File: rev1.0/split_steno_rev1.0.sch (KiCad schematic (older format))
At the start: 45 parts, among them J0 Audio-Jack-4, K0 KEYSW, K1 KEYSW, K10 KEYSW, K11 KEYSW, K12 KEYSW, K13 KEYSW, K14 KEYSW, K15 KEYSW, K16 KEYSW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

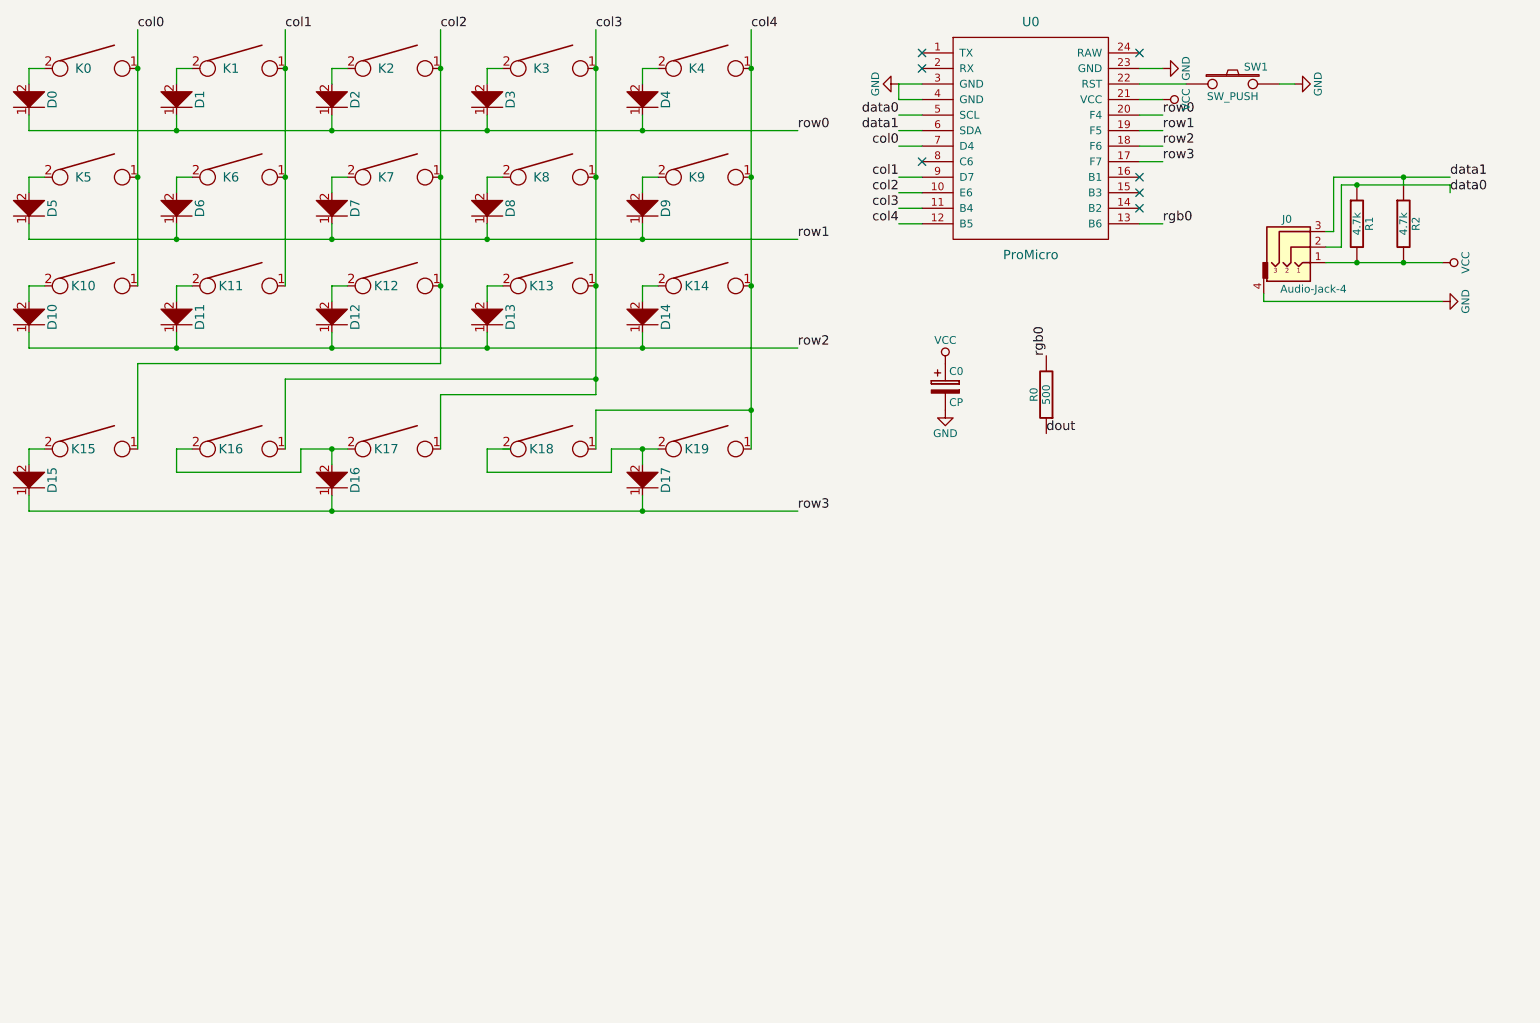
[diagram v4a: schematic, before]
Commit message: updated schematic and footprints
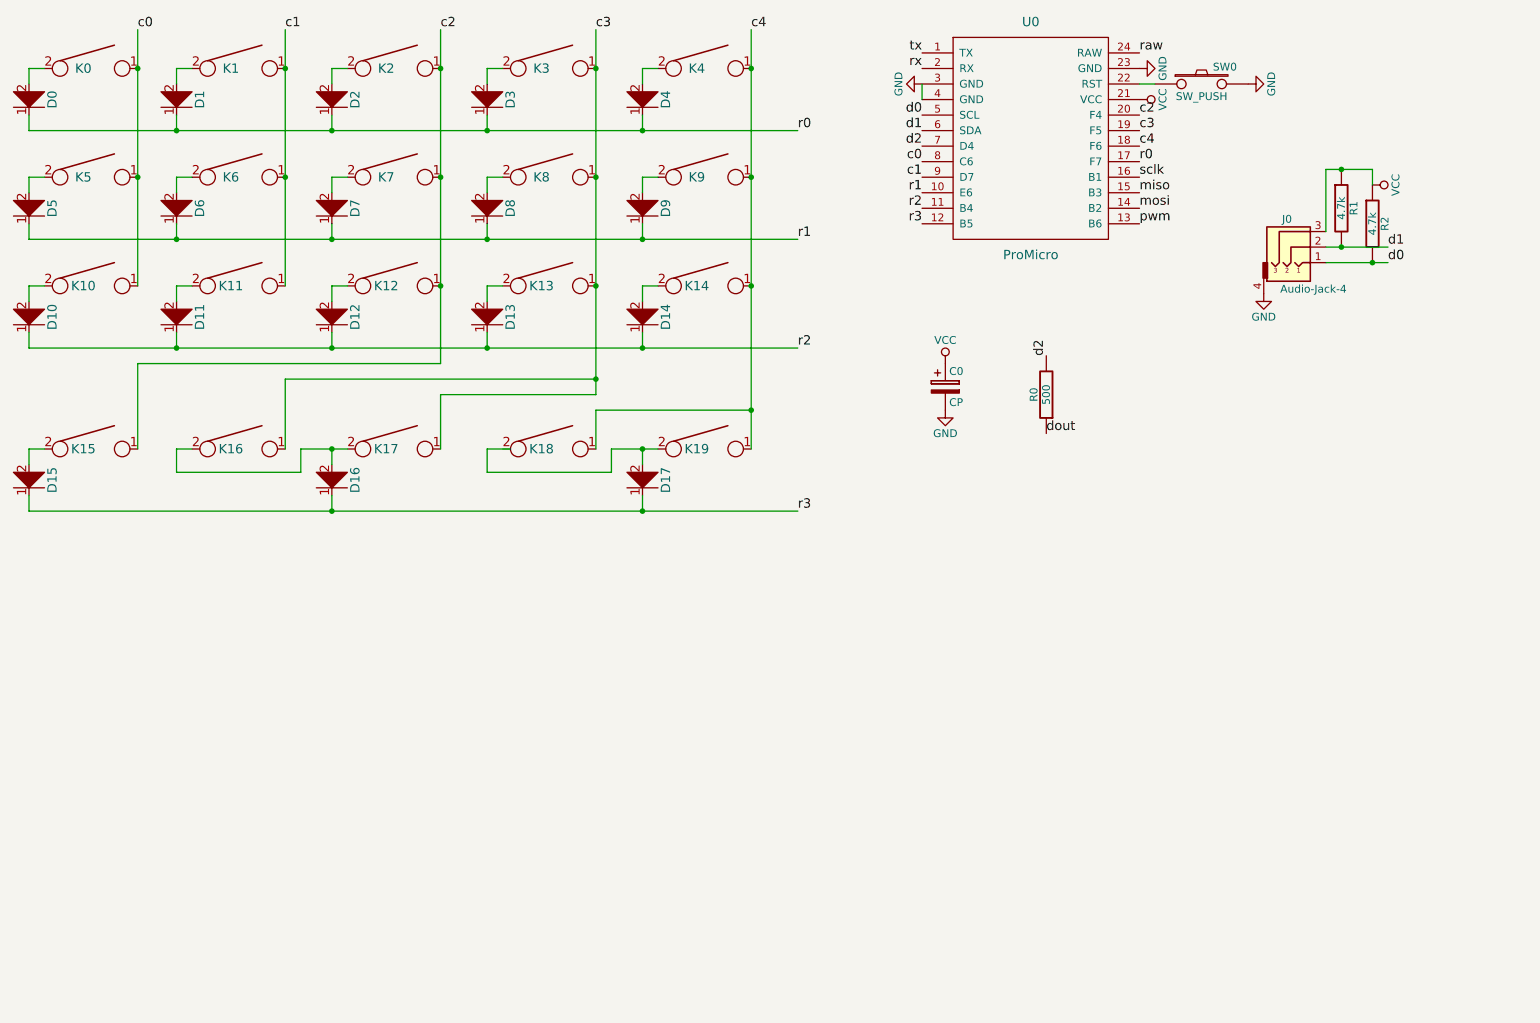
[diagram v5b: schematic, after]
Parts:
- C0: footprint Capacitors_THT:CP_Radial_D5.0mm_P2.50mm -> Capacitors_THT:CP_Radial_D4.0mm_P2.00mm
- J0: footprint Keebio-Parts:TRRS-PJ-320A-dual -> Keebio-Parts:TRRS-PJ-320A
- K16, K18: footprint Keebio-Parts:Hybrid_PCB_200H-dual -> Keebio-Parts:Hybrid_PCB_200H-dual-nosilk
- renumbered SW1 to SW0
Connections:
- net VCC: now also J0.3, R1.1, R2.1; no longer J0.1, R1.2, R2.2
- net tx: now reaches U0.1 (TX)
- net mosi: now reaches U0.14 (B2)
- net miso: now reaches U0.15 (B3)
- net sclk: now reaches U0.16 (B1)
- net rx: now reaches U0.2 (RX)
- net raw: now reaches U0.24 (RAW)
- net c0: now reaches U0.8 (C6)
- net c0: now also K0.1, K10.1, K5.1
- removed net col0: K0.1, K10.1, K5.1, U0.7 (D4)
- net col1 renamed c1
- net col2 renamed c2
- net c2: now also U0.20 (F4); no longer U0.10 (E6)
- net col3 renamed c3
- net c3: now also U0.19 (F5); no longer U0.11 (B4)
- net col4 renamed c4
- net c4: now also U0.18 (F6); no longer U0.12 (B5)
- removed net data0: J0.2, R1.1, U0.5 (SCL)
- removed net data1: J0.3, R2.1, U0.6 (SDA)
- net rgb0 renamed d2
- net d2: now also U0.7 (D4); no longer U0.13 (B6)
- net row0 renamed r0
- net r0: now also U0.17 (F7); no longer U0.20 (F4)
- net row1 renamed r1
- net r1: now also U0.10 (E6); no longer U0.19 (F5)
- net row2 renamed r2
- net r2: now also U0.11 (B4); no longer U0.18 (F6)
- net row3 renamed r3
- net r3: now also U0.12 (B5); no longer U0.17 (F7)
- new net d0: J0.1, R2.2, U0.5 (SCL)
- new net d1: J0.2, R1.2, U0.6 (SDA)
- new net pwm: U0.13 (B6)
- no-connect marks 7 -> 0
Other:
- moved on the sheet: R1, R2, SW0
